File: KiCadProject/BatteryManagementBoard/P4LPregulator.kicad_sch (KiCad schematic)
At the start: 4 parts, among them U401 BD433M5FP

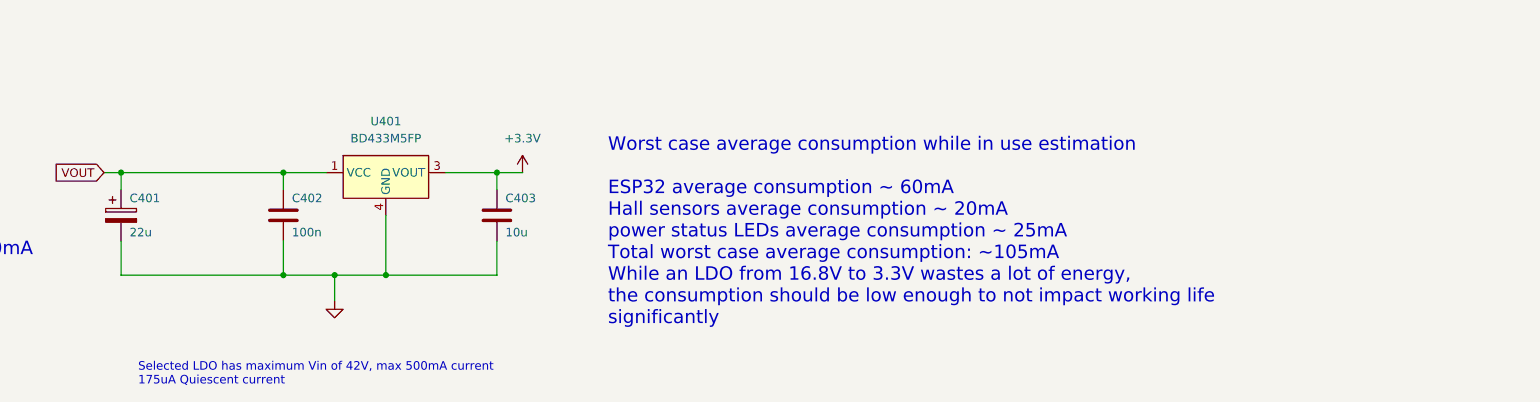
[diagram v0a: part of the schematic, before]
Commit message: ESP board layout mostly done. Small updates to battery management board
Signed-off-by: Eldalote.Electronics <Eldalote.Electronics@gmail.com>
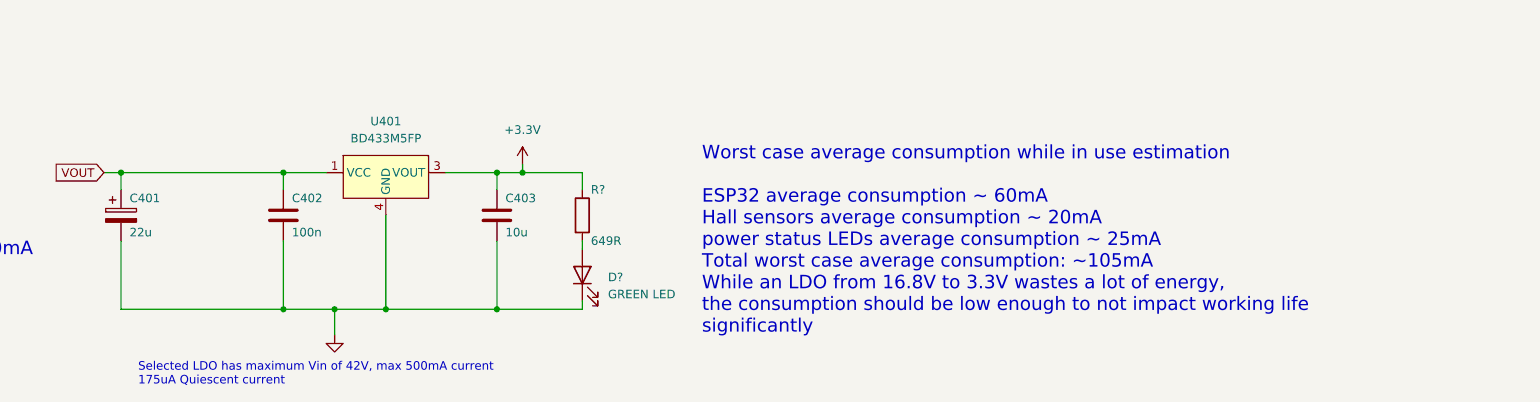
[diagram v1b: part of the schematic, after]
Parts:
- added D?: GREEN LED, symbol Device:LED
- added R?: 649R, symbol Device:R
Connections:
- net +3.3V: now also R?.1
- net GND: now also D?.1 (K)
- new net: D?.2 (A), R?.2
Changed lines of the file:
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@@
   (junction (at 151.13 91.44) (diameter 0) (color 0 0 0 0)
   )
+  (junction (at 151.13 111.76) (diameter 0) (color 0 0 0 0)
+  )
   (junction (at 119.38 91.44) (diameter 0) (color 0 0 0 0)
   )
-  (junction (at 127 106.68) (diameter 0) (color 0 0 0 0)
-  )
-  (junction (at 119.38 106.68) (diameter 0) (color 0 0 0 0)
-  )
-  (junction (at 134.62 106.68) (diameter 0) (color 0 0 0 0)
-  )
-  (wire (pts (xy 119.38 101.6) (xy 119.38 106.68))
+  (junction (at 127 111.76) (diameter 0) (color 0 0 0 0)
+  )
+  (junction (at 119.38 111.76) (diameter 0) (color 0 0 0 0)
+  )
+  (junction (at 134.62 111.76) (diameter 0) (color 0 0 0 0)
+  )
+  (junction (at 154.94 91.44) (diameter 0) (color 0 0 0 0)
+  )
+  (wire (pts (xy 119.38 101.6) (xy 119.38 111.76))
     (stroke (width 0) (type default) (color 0 0 0 0))
   )
@@
     (stroke (width 0) (type default) (color 0 0 0 0))
   )
-  (wire (pts (xy 127 106.68) (xy 127 110.49))
+  (wire (pts (xy 163.83 91.44) (xy 154.94 91.44))
+    (stroke (width 0) (type default) (color 0 0 0 0))
+  )
+  (wire (pts (xy 127 111.76) (xy 127 115.57))
     (stroke (width 0) (type default) (color 0 0 0 0))
   )
@@
     (stroke (width 0) (type default) (color 0 0 0 0))
   )
-  (wire (pts (xy 134.62 97.79) (xy 134.62 106.68))
-    (stroke (width 0) (type default) (color 0 0 0 0))
-  )
-  (wire (pts (xy 151.13 106.68) (xy 134.62 106.68))
-    (stroke (width 0) (type default) (color 0 0 0 0))
-  )
-  (wire (pts (xy 95.25 101.6) (xy 95.25 106.68))
-    (stroke (width 0) (type default) (color 0 0 0 0))
-  )
-  (wire (pts (xy 151.13 101.6) (xy 151.13 106.68))
-    (stroke (width 0) (type default) (color 0 0 0 0))
-  )
-  (wire (pts (xy 95.25 106.68) (xy 119.38 106.68))
+  (wire (pts (xy 151.13 101.6) (xy 151.13 111.76))
+    (stroke (width 0) (type default) (color 0 0 0 0))
+  )
+  (wire (pts (xy 163.83 111.76) (xy 151.13 111.76))
+    (stroke (width 0) (type default) (color 0 0 0 0))
+  )
+  (wire (pts (xy 163.83 93.98) (xy 163.83 91.44))
+    (stroke (width 0) (type default) (color 0 0 0 0))
+  )
+  (wire (pts (xy 151.13 111.76) (xy 134.62 111.76))
+    (stroke (width 0) (type default) (color 0 0 0 0))
+  )
+  (wire (pts (xy 163.83 110.49) (xy 163.83 111.76))
+    (stroke (width 0) (type default) (color 0 0 0 0))
+  )
+  (wire (pts (xy 154.94 90.17) (xy 154.94 91.44))
+    (stroke (width 0) (type default) (color 0 0 0 0))
+  )
+  (wire (pts (xy 95.25 111.76) (xy 119.38 111.76))
     (stroke (width 0) (type default) (color 0 0 0 0))
   )
@@
     (stroke (width 0) (type default) (color 0 0 0 0))
   )
+  (wire (pts (xy 95.25 101.6) (xy 95.25 111.76))
+    (stroke (width 0) (type default) (color 0 0 0 0))
+  )
+  (wire (pts (xy 163.83 101.6) (xy 163.83 102.87))
+    (stroke (width 0) (type default) (color 0 0 0 0))
+  )
   (wire (pts (xy 92.71 91.44) (xy 95.25 91.44))
     (stroke (width 0) (type default) (color 0 0 0 0))
   )
-  (wire (pts (xy 134.62 106.68) (xy 127 106.68))
-    (stroke (width 0) (type default) (color 0 0 0 0))
-  )
-  (wire (pts (xy 127 106.68) (xy 119.38 106.68))
+  (wire (pts (xy 134.62 111.76) (xy 127 111.76))
+    (stroke (width 0) (type default) (color 0 0 0 0))
+  )
+  (wire (pts (xy 127 111.76) (xy 119.38 111.76))
+    (stroke (width 0) (type default) (color 0 0 0 0))
+  )
+  (wire (pts (xy 134.62 97.79) (xy 134.62 111.76))
     (stroke (width 0) (type default) (color 0 0 0 0))
   )
@@
   )
   (text "Worst case average consumption while in use estimation\n\nESP32 average consumption ~ 60mA\nHall sensors average consumption ~ 20mA\npower status LEDs average consumption ~ 25mA\nTotal worst case average consumption: ~105mA\nWhile an LDO from 16.8V to 3.3V wastes a lot of energy,\nthe consumption should be low enough to not impact working life\nsignificantly"
-    (at 167.64 114.3 0)
+    (at 181.61 115.57 0)
     (effects (font (size 2 2)) (justify left bottom))
   )
@@
     )
   )
+  (symbol (lib_id "Device:LED") (at 163.83 106.68 90) (unit 1)
+    (in_bom yes) (on_board yes) (fields_autoplaced)
+    (property "Reference" "D?" (id 0) (at 167.64 106.9974 90)
+      (effects (font (size 1.27 1.27)) (justify right))
+    )
+    (property "Value" "GREEN LED" (id 1) (at 167.64 109.5374 90)
+      (effects (font (size 1.27 1.27)) (justify right))
+    )
+    (property "Footprint" "" (id 2) (at 163.83 106.68 0)
+      (effects (font (size 1.27 1.27)) hide)
+    )
+    (property "Datasheet" "~" (id 3) (at 163.83 106.68 0)
+      (effects (font (size 1.27 1.27)) hide)
+    )
+    (pin "1")
+    (pin "2")
+  )
   (symbol (lib_id "Eldalote_symbols:BD433M5FP") (at 134.62 91.44 0) (unit 1)
     (in_bom yes) (on_board yes) (fields_autoplaced)
@@
     (pin "4")
   )
-  (symbol (lib_id "power:+3.3V") (at 154.94 91.44 0) (unit 1)
-    (in_bom yes) (on_board yes) (fields_autoplaced)
-    (property "Reference" "#PWR0602" (id 0) (at 154.94 95.25 0)
-      (effects (font (size 1.27 1.27)) hide)
-    )
-    (property "Value" "+3.3V" (id 1) (at 154.94 86.36 0))
-    (property "Footprint" "" (id 2) (at 154.94 91.44 0)
-      (effects (font (size 1.27 1.27)) hide)
-    )
-    (property "Datasheet" "" (id 3) (at 154.94 91.44 0)
+  (symbol (lib_id "power:+3.3V") (at 154.94 90.17 0) (unit 1)
+    (in_bom yes) (on_board yes) (fields_autoplaced)
+    (property "Reference" "#PWR0602" (id 0) (at 154.94 93.98 0)
+      (effects (font (size 1.27 1.27)) hide)
+    )
+    (property "Value" "+3.3V" (id 1) (at 154.94 85.09 0))
+    (property "Footprint" "" (id 2) (at 154.94 90.17 0)
+      (effects (font (size 1.27 1.27)) hide)
+    )
+    (property "Datasheet" "" (id 3) (at 154.94 90.17 0)
       (effects (font (size 1.27 1.27)) hide)
     )
@@
     (pin "2")
   )
-  (symbol (lib_id "power:GND") (at 127 110.49 0) (unit 1)
-    (in_bom yes) (on_board yes) (fields_autoplaced)
-    (property "Reference" "#PWR0601" (id 0) (at 127 116.84 0)
-      (effects (font (size 1.27 1.27)) hide)
-    )
-    (property "Value" "GND" (id 1) (at 127 115.57 0)
-      (effects (font (size 1.27 1.27)) hide)
-    )
-    (property "Footprint" "" (id 2) (at 127 110.49 0)
-      (effects (font (size 1.27 1.27)) hide)
-    )
-    (property "Datasheet" "" (id 3) (at 127 110.49 0)
-      (effects (font (size 1.27 1.27)) hide)
-    )
-    (pin "1")
+  (symbol (lib_id "power:GND") (at 127 115.57 0) (unit 1)
+    (in_bom yes) (on_board yes) (fields_autoplaced)
+    (property "Reference" "#PWR0601" (id 0) (at 127 121.92 0)
+      (effects (font (size 1.27 1.27)) hide)
+    )
+    (property "Value" "GND" (id 1) (at 127 120.65 0)
+      (effects (font (size 1.27 1.27)) hide)
+    )
+    (property "Footprint" "" (id 2) (at 127 115.57 0)
+      (effects (font (size 1.27 1.27)) hide)
+    )
+    (property "Datasheet" "" (id 3) (at 127 115.57 0)
+      (effects (font (size 1.27 1.27)) hide)
+    )
+    (pin "1")
+  )
+  (symbol (lib_id "Device:R") (at 163.83 97.79 0) (unit 1)
+    (in_bom yes) (on_board yes)
+    (property "Reference" "R?" (id 0) (at 165.1 93.98 0)
+      (effects (font (size 1.27 1.27)) (justify left))
+    )
+    (property "Value" "649R" (id 1) (at 165.1 101.6 0)
+      (effects (font (size 1.27 1.27)) (justify left))
+    )
+    (property "Footprint" "" (id 2) (at 162.052 97.79 90)
+      (effects (font (size 1.27 1.27)) hide)
+    )
+    (property "Datasheet" "~" (id 3) (at 163.83 97.79 0)
+      (effects (font (size 1.27 1.27)) hide)
+    )
+    (pin "1")
+    (pin "2")
   )
   (symbol (lib_id "Device:C") (at 151.13 97.79 0) (unit 1)

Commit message: Tweaking
Signed-off-by: Eldalote.Electronics <Eldalote.Electronics@gmail.com>
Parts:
- R401: renamed from R?; footprint (none) -> Resistor_SMD:R_0402_1005Metric
- gave numbers to parts that had none: 1
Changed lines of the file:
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@@
   (junction (at 151.13 91.44) (diameter 0) (color 0 0 0 0)
   )
+  (junction (at 162.56 91.44) (diameter 0) (color 0 0 0 0)
+  )
   (junction (at 151.13 111.76) (diameter 0) (color 0 0 0 0)
   )
@@
     (stroke (width 0) (type default) (color 0 0 0 0))
   )
+  (wire (pts (xy 162.56 91.44) (xy 154.94 91.44))
+    (stroke (width 0) (type default) (color 0 0 0 0))
+  )
   (wire (pts (xy 119.38 91.44) (xy 119.38 93.98))
     (stroke (width 0) (type default) (color 0 0 0 0))
@@
     (stroke (width 0) (type default) (color 0 0 0 0))
   )
-  (wire (pts (xy 163.83 91.44) (xy 154.94 91.44))
+  (wire (pts (xy 163.83 91.44) (xy 162.56 91.44))
     (stroke (width 0) (type default) (color 0 0 0 0))
   )
@@
   (symbol (lib_id "Device:LED") (at 163.83 106.68 90) (unit 1)
     (in_bom yes) (on_board yes) (fields_autoplaced)
-    (property "Reference" "D?" (id 0) (at 167.64 106.9974 90)
+    (property "Reference" "D401" (id 0) (at 167.64 106.9974 90)
       (effects (font (size 1.27 1.27)) (justify right))
     )
@@
   (symbol (lib_id "power:+3.3V") (at 154.94 90.17 0) (unit 1)
     (in_bom yes) (on_board yes) (fields_autoplaced)
-    (property "Reference" "#PWR0602" (id 0) (at 154.94 93.98 0)
+    (property "Reference" "#PWR0402" (id 0) (at 154.94 93.98 0)
       (effects (font (size 1.27 1.27)) hide)
     )
@@
   (symbol (lib_id "power:GND") (at 127 115.57 0) (unit 1)
     (in_bom yes) (on_board yes) (fields_autoplaced)
-    (property "Reference" "#PWR0601" (id 0) (at 127 121.92 0)
+    (property "Reference" "#PWR0401" (id 0) (at 127 121.92 0)
       (effects (font (size 1.27 1.27)) hide)
     )
@@
     )
     (property "Datasheet" "" (id 3) (at 127 115.57 0)
+      (effects (font (size 1.27 1.27)) hide)
+    )
+    (pin "1")
+  )
+  (symbol (lib_id "power:PWR_FLAG") (at 162.56 91.44 0) (unit 1)
+    (in_bom yes) (on_board yes)
+    (property "Reference" "#FLG0401" (id 0) (at 162.56 89.535 0)
+      (effects (font (size 1.27 1.27)) hide)
+    )
+    (property "Value" "PWR_FLAG" (id 1) (at 162.56 87.63 0)
+      (effects (font (size 1.27 1.27)) hide)
+    )
+    (property "Footprint" "" (id 2) (at 162.56 91.44 0)
+      (effects (font (size 1.27 1.27)) hide)
+    )
+    (property "Datasheet" "~" (id 3) (at 162.56 91.44 0)
       (effects (font (size 1.27 1.27)) hide)
     )
@@
   (symbol (lib_id "Device:R") (at 163.83 97.79 0) (unit 1)
     (in_bom yes) (on_board yes)
-    (property "Reference" "R?" (id 0) (at 165.1 93.98 0)
+    (property "Reference" "R401" (id 0) (at 165.1 93.98 0)
       (effects (font (size 1.27 1.27)) (justify left))
     )
@@
       (effects (font (size 1.27 1.27)) (justify left))
     )
-    (property "Footprint" "" (id 2) (at 162.052 97.79 90)
-      (effects (font (size 1.27 1.27)) hide)
-    )
+    (property "Footprint" "Resistor_SMD:R_0402_1005Metric" (id 2) (at 162.052 97.79 90)
+      (effects (font (size 1.27 1.27)) hide)
+    )

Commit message: Final touches before component order and PCB layout
Signed-off-by: Eldalote.Electronics <Eldalote.Electronics@gmail.com>
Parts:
- D401: footprint (none) -> LED_SMD:LED_0603_1608Metric
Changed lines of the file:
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@@
       (effects (font (size 1.27 1.27)) (justify right))
     )
-    (property "Footprint" "" (id 2) (at 163.83 106.68 0)
+    (property "Footprint" "LED_SMD:LED_0603_1608Metric" (id 2) (at 163.83 106.68 0)
       (effects (font (size 1.27 1.27)) hide)
     )

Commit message: Components selected, MfID added to schematics, and components ordered
Signed-off-by: Eldalote.Electronics <Eldalote.Electronics@gmail.com>
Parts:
- C401: MfID (none) -> 865080542006
- C402: Extra Requirement (none) -> 25V; MfID (none) -> CL05A104KA5NNNC
- C403: Extra Requirement (none) -> 25V; MfID (none) -> CL21A106KAYNNNG
- D401: footprint LED_SMD:LED_0603_1608Metric -> LED_SMD:LED_0805_2012Metric; MfID (none) -> APT2012CGCK
- R401: MfID (none) -> RC0402FR-07649RL
- U401: MfID (none) -> BD433M5FP-CE2
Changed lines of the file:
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@@
       (effects (font (size 1.27 1.27)) (justify right))
     )
-    (property "Footprint" "LED_SMD:LED_0603_1608Metric" (id 2) (at 163.83 106.68 0)
+    (property "Footprint" "LED_SMD:LED_0805_2012Metric" (id 2) (at 163.83 106.68 0)
       (effects (font (size 1.27 1.27)) hide)
     )
     (property "Datasheet" "~" (id 3) (at 163.83 106.68 0)
+      (effects (font (size 1.27 1.27)) hide)
+    )
+    (property "MfID" "APT2012CGCK" (id 4) (at 163.83 106.68 0)
       (effects (font (size 1.27 1.27)) hide)
     )
@@
     )
     (property "Datasheet" "" (id 3) (at 134.62 91.44 0)
+      (effects (font (size 1.27 1.27)) hide)
+    )
+    (property "MfID" "BD433M5FP-CE2" (id 4) (at 134.62 91.44 0)
       (effects (font (size 1.27 1.27)) hide)
     )
@@
     )
     (property "Datasheet" "~" (id 3) (at 95.25 97.79 0)
+      (effects (font (size 1.27 1.27)) hide)
+    )
+    (property "MfID" "865080542006" (id 4) (at 95.25 97.79 0)
       (effects (font (size 1.27 1.27)) hide)
     )
@@
       (effects (font (size 1.27 1.27)) hide)
     )
+    (property "MfID" "RC0402FR-07649RL" (id 4) (at 163.83 97.79 0)
+      (effects (font (size 1.27 1.27)) hide)
+    )
     (pin "1")
     (pin "2")
@@
     )
     (property "Datasheet" "~" (id 3) (at 151.13 97.79 0)
+      (effects (font (size 1.27 1.27)) hide)
+    )
+    (property "Extra Requirement" "25V" (id 4) (at 151.13 97.79 0)
+      (effects (font (size 1.27 1.27)) hide)
+    )
+    (property "MfID" "CL21A106KAYNNNG" (id 5) (at 151.13 97.79 0)
       (effects (font (size 1.27 1.27)) hide)
     )
@@
       (effects (font (size 1.27 1.27)) hide)
     )
+    (property "Extra Requirement" "25V" (id 4) (at 119.38 97.79 0)
+      (effects (font (size 1.27 1.27)) hide)
+    )
+    (property "MfID" "CL05A104KA5NNNC" (id 5) (at 119.38 97.79 0)
+      (effects (font (size 1.27 1.27)) hide)
+    )

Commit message: Layout on the battery management board
Signed-off-by: Eldalote.Electronics <Eldalote.Electronics@gmail.com>
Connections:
- net POWER_LED: now reaches D401.2 (A), R401.2
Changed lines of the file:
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@@
     (effects (font (size 4 4) (thickness 0.8) bold) (justify left bottom))
+  )
+  (label "POWER_LED" (at 163.83 101.6 0)
+    (effects (font (size 0.5 0.5)) (justify left bottom))
   )
   (global_label "VOUT" (shape input) (at 92.71 91.44 180) (fields_autoplaced)
